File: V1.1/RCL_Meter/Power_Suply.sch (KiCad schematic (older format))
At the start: 25 parts

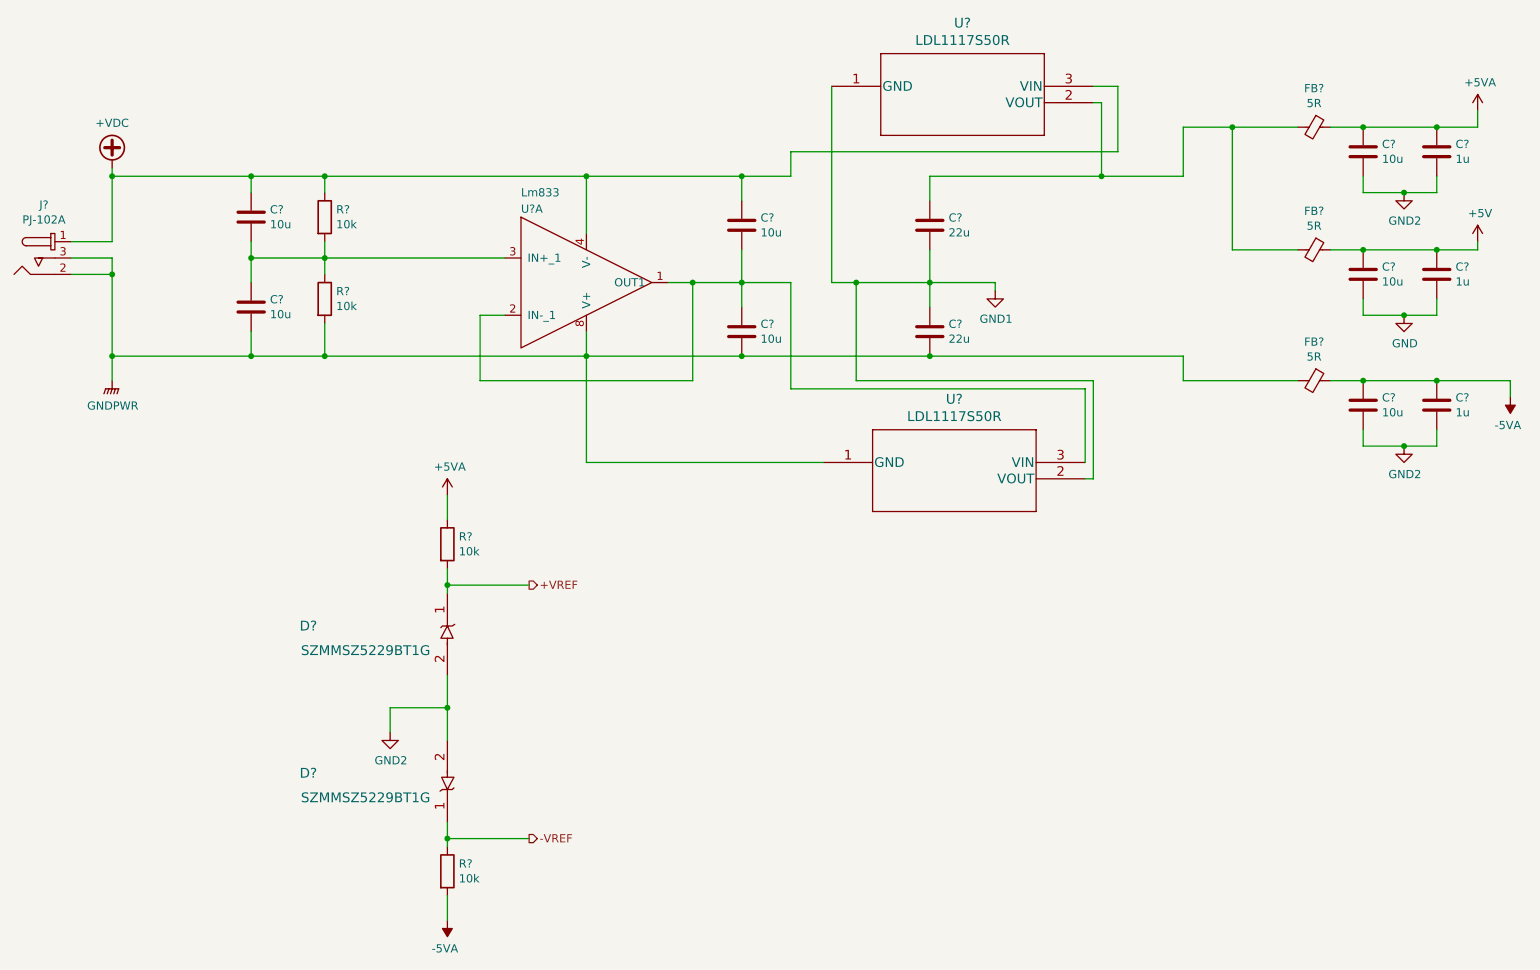
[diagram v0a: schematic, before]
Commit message: Added USB Support
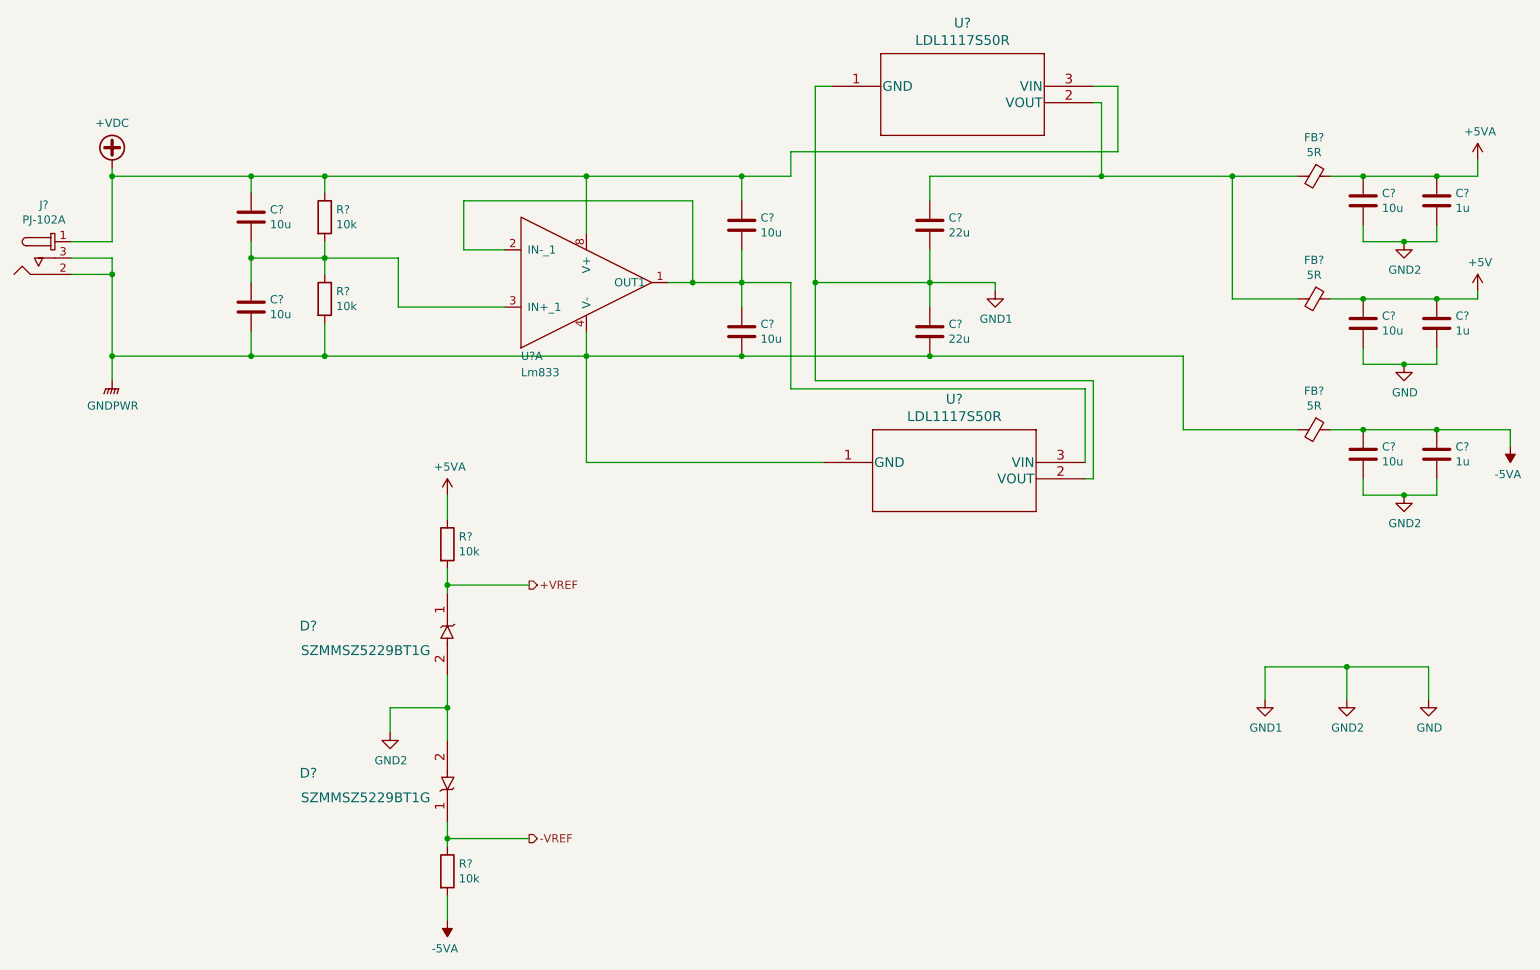
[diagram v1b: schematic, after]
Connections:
- net GND1 is gone; now on net GND: C?.1, C?.2, U?.1 (GND), U?.2 (VOUT)
- net GND2 is gone; now on net GND: C?.2, C?.2, C?.2, C?.2, D?.2, D?.2
- net +VDC: now also U?.8 (V+); no longer U?.4 (V-)
- net GNDPWR: now also U?.4 (V-); no longer U?.8 (V+)
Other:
- moved on the sheet: C?, FB?
